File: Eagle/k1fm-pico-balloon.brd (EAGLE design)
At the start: 26.4 x 41.1 mm, 40 parts, among them Q1 ASTX-H11-25.000MHZ-T, Q2 DMP2305U, Q3 DMP2305U, U1 ATMEGA328, U2 Si5351A-B-GT, U3 MCP1754X-XXXXX/C, U4 TMP36, Y1 8/16/20MHz

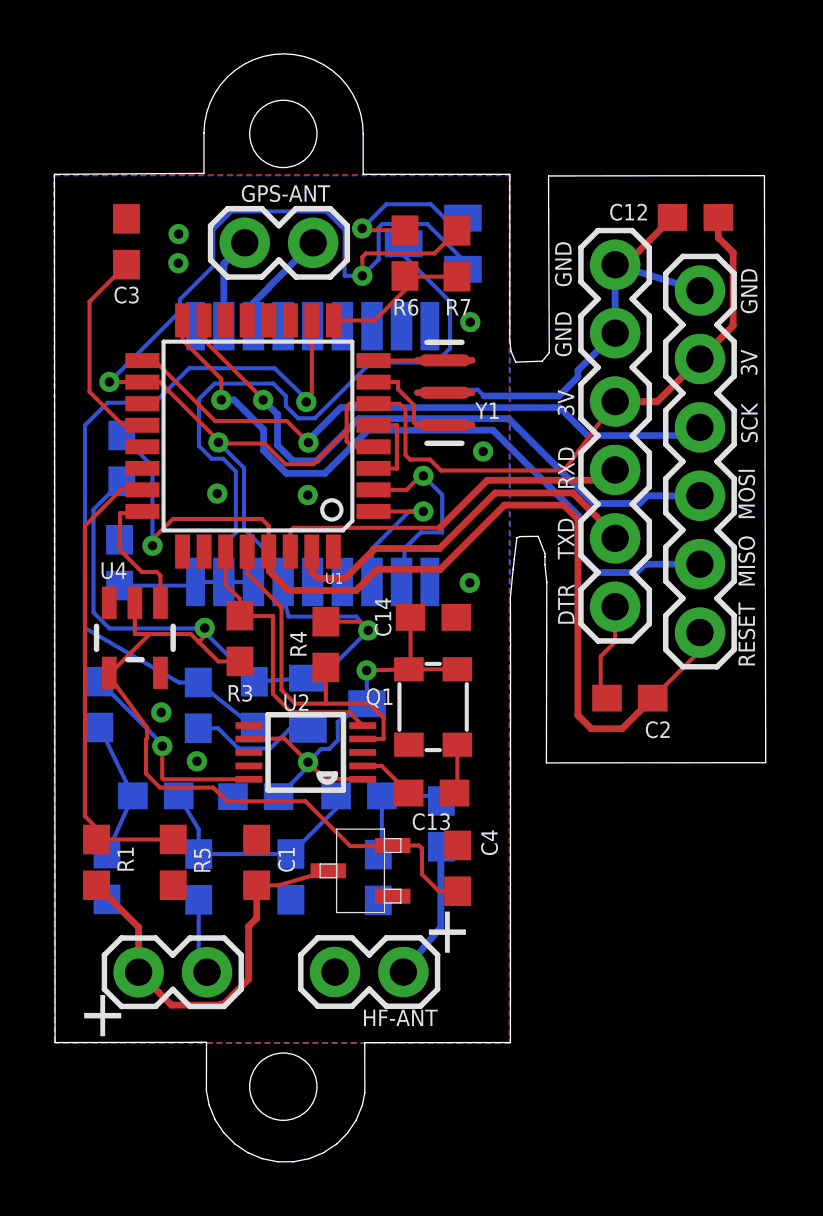
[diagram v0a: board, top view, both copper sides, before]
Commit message: 4 Layers. Added external SCL, SDA, GPS lines.
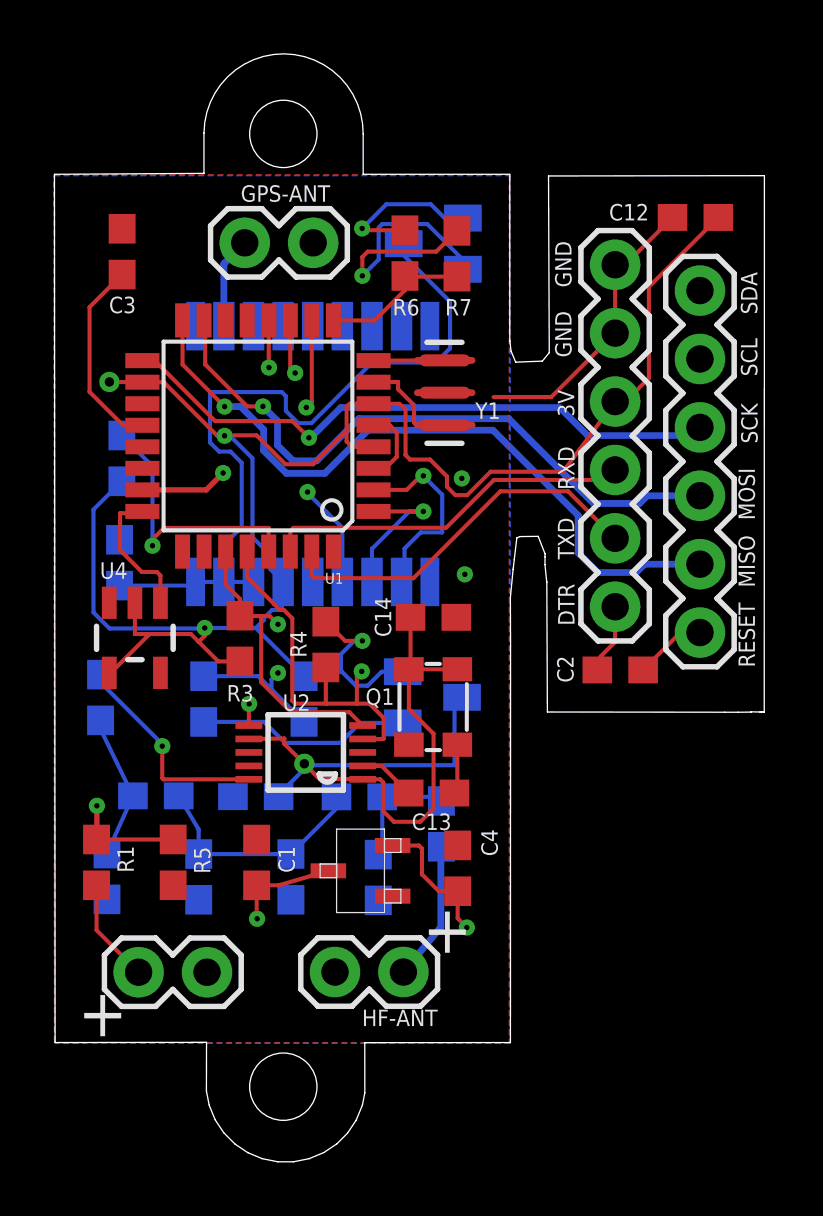
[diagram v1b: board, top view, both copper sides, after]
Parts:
- moved Q3 3.53 mm to (13.0, 60.6)
- moved R9 1.86 mm to (8.27, 60.5)
- moved C2 1.11 mm to (20.0, 61.6)
- moved C3 0.40 mm to (1.51, 77.1)
- moved R8 0.31 mm to (4.55, 60.5)
- moved L1 0.27 mm to (0.71, 60.6)
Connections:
- new net B0: GPS1.4_TIMEPULSE, U1.12
- new net D7: U1.11, U2.6
- net 3V: no longer J3.2
- net GND: no longer J3.1
- net SCL: now also J3.2
- net SDA: now also J3.1
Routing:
- net SDA: track 10.5 -> 36.1 mm, vias 0 -> 1
- net SCL: track 12.8 -> 36.4 mm, vias 0 -> 1
- net D7: track 0.00 -> 16.3 mm, vias 0 -> 2
- net GND: track 27.1 -> 13.8 mm, vias 9 -> 2
- net N$15: track 16.6 -> 28.2 mm, vias 2 -> 1
- net B0: track 0.00 -> 10.8 mm, vias 0 -> 2
- net TX_E: track 27.8 -> 19.9 mm, vias 1 -> 2
- net N$4: track 17.4 -> 22.1 mm, vias 0 -> 2
- net N$7: track 4.68 -> 8.02 mm
- net VDD: track 15.2 -> 13.2 mm, vias 0 -> 1
- net DTR: track 3.71 -> 2.62 mm
- net N$12: track 5.19 -> 6.26 mm
- net 3V: track 118.2 -> 118.4 mm, vias 5 -> 6
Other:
- outline, holes or cut-outs redrawn
- board text added: "K1FM v 1.3"
- board text added: "SCL"
- board text added: "SDA"
- board text removed: "K1FM v 1.2"

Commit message: Reorganized TX/RX lines - Conn layout
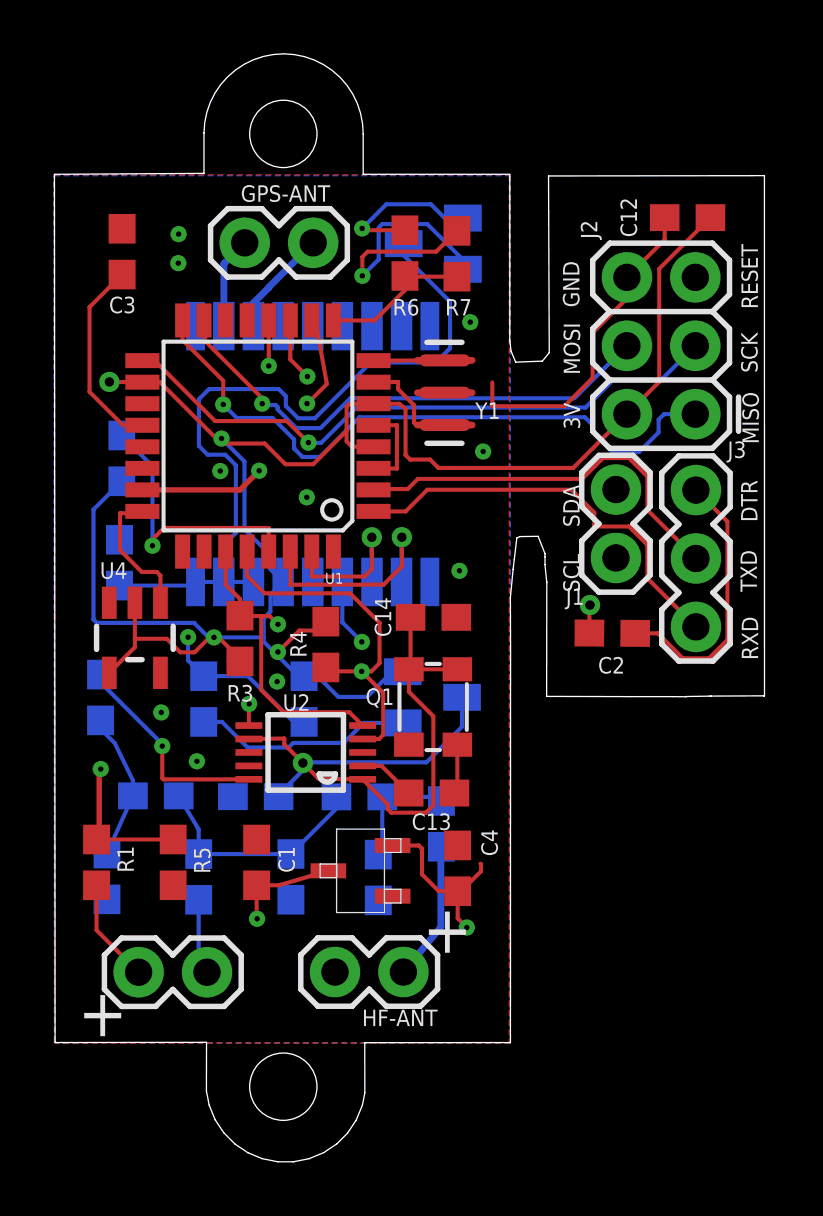
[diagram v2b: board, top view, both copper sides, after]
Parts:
- added J1: I2C, SparkFun-Connectors:1X02
- J2: value (none) -> ICSP; device SparkFun-Connectors:1X06 -> SparkFun-Connectors:2X3
- J3: value (none) -> SERIAL; device SparkFun-Connectors:1X06 -> SparkFun-Connectors:1X03
- moved J2 7.75 mm to (22.8, 71.1)
- moved J3 7.41 mm to (22.8, 68.3)
- moved C2 1.39 mm to (19.7, 63.0), turned to 179.6 degrees
- moved C12 0.29 mm to (22.5, 78.4)
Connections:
- net B0 renamed TIMEP
- net D7 renamed CLK2
- removed net D3: GPS1.3_RXD1, U1.1
- removed net D4: GPS1.2_TXD1, U1.2
- new net RXD: GPS1.2_TXD1, U1.30
- new net TXD: GPS1.3_RXD1, U1.31
- net 3V: now also J2.2; no longer J2.4
- net DTR: now also J3.1; no longer J2.1
- net GND: no longer J2.5
- net MISO: now also J2.1; no longer J3.5
- net MOSI: now also J2.4; no longer J3.4
- net RESET: now also J2.5; no longer J3.6
- net RXI: now also J3.3, U1.1; no longer J2.3, U1.30
- net SCK: now also J2.3; no longer J3.3
- net SCL: now also J1.2; no longer J3.2
- net SDA: now also J1.1; no longer J3.1
- net TXO: now also J3.2, U1.2; no longer J2.2, U1.31
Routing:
- net 3V: track 118.4 -> 139.0 mm
- net TIMEP: track 10.8 -> 24.6 mm
- net GND: track 13.8 -> 23.7 mm, vias 2 -> 10
- net SDA: track 36.1 -> 26.6 mm
- net SCL: track 36.4 -> 27.5 mm
- net TX_E: track 19.9 -> 28.6 mm
- net RXD: track 0.00 -> 8.56 mm, vias 0 -> 1
- net DTR: track 2.62 -> 10.1 mm
- net D4: track 7.39 -> 0.00 mm, vias 1 -> 0
- net TXD: track 0.00 -> 6.09 mm, vias 0 -> 1
- net RESET: track 38.4 -> 44.2 mm, vias 1 -> 2
- net D3: track 5.56 -> 0.00 mm, vias 1 -> 0
- net MOSI: track 24.1 -> 19.2 mm
- net MISO: track 26.8 -> 24.4 mm
- net N$4: track 22.1 -> 24.2 mm
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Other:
- outline, holes or cut-outs redrawn
- board text removed: "RST"
- board text removed: "VCC"

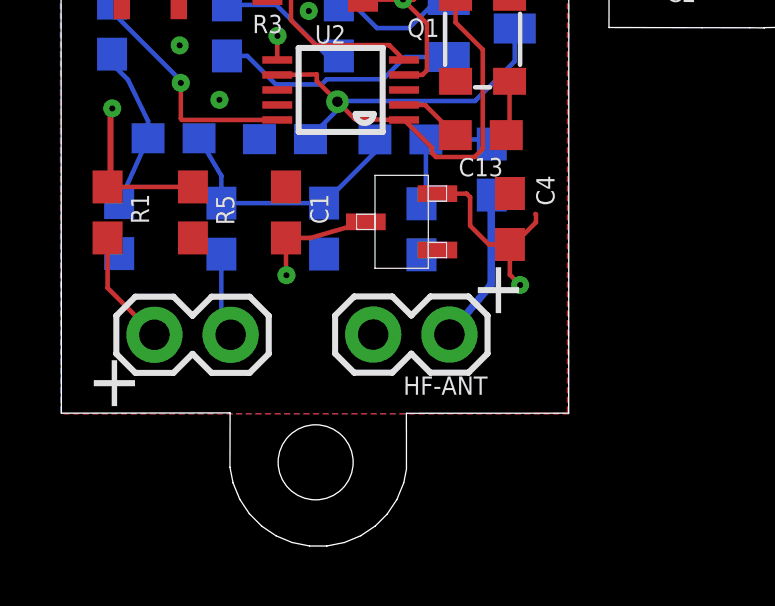
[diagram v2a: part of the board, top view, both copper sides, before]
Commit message: Add diode and connection for direct solar power
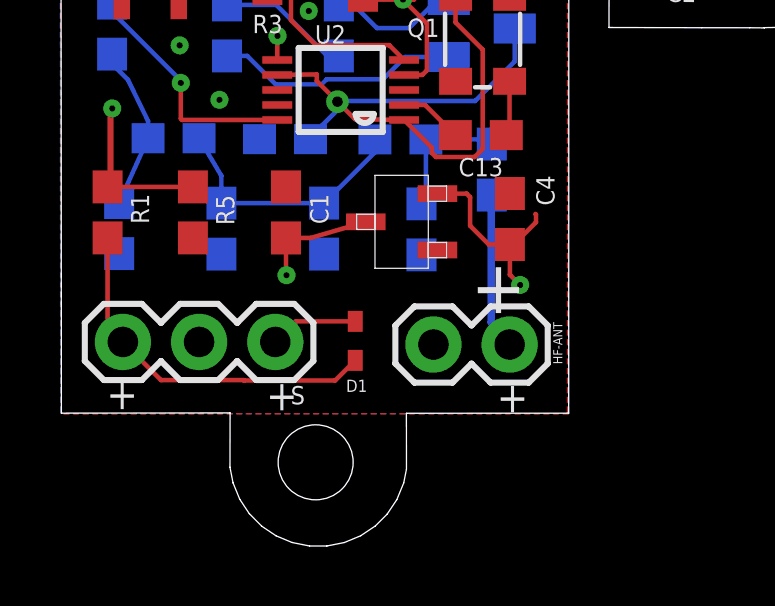
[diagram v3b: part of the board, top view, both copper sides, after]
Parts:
- removed 3.3V: 3.3V, SparkFun-Connectors:1X02
- added D1: 1N4148X-TP, diode:SOD523
- added J4: POWER, SparkFun-Connectors:1X03
- moved HF-ANT 2.03 mm to (14.0, 50.0)
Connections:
- new net N$3: D1.A, J4.3
- net GND: now also J4.2; no longer 3.3V.2
- net VDD: now also D1.C, J4.1; no longer 3.3V.1
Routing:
- net VDD: track 13.2 -> 22.7 mm
- net N$3: track 0.00 -> 2.95 mm
- net GND: track 23.7 -> 20.9 mm
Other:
- board text added: "S"
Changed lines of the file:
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@@
 <wire x1="4.553053125" y1="80.0339625" x2="-1" y2="80" width="0" layer="20"/>
 <wire x1="-1" y1="80" x2="-0.975784375" y2="47.755840625" width="0" layer="20"/>
-<text x="-0.12739375" y="47.991096875" size="1.778" layer="25">+</text>
+<text x="0.5252" y="47.889196875" size="1.016" layer="25">+</text>
 <text x="21.36460625" y="70.45336875" size="1.27" layer="26" rot="MR270" align="center">REMOVE
 BEFORE
 FLIGHT</text>
-<text x="13.09675" y="49.125609375" size="1.016" layer="26" rot="MR90">K1FM
+<text x="12.892821875" y="52.08070625" size="1.016" layer="26" rot="MR90">K1FM
 v 1.3</text>
 <wire x1="4.553053125" y1="80.0339625" x2="4.553053125" y2="81.5339625" width="0" layer="20"/>
@@
 <hole x="7.4994125" y="46.1168625" drill="2.5"/>
 <text x="12.67260625" y="51.091096875" size="1.778" layer="25">+</text>
+<text x="5.847759375" y="47.848434375" size="1.016" layer="25">+</text>
+<text x="13.5358875" y="47.787309375" size="1.016" layer="25">+</text>
+<text x="6.666075" y="48.049109375" size="0.6096" layer="21">S</text>
 </plain>
 <attributes>
@@
 </element>
 <element name="C7" library="SparkFun-Capacitors" library_urn="urn:adsk.eagle:library:510" package="0603" package3d_urn="urn:adsk.eagle:package:37414/1" value="47pF" x="7.7810625" y="53.907934375" smashed="yes" rot="MR90">
-<attribute name="NAME" x="7.795859375" y="51.543271875" size="0.6096" layer="26" font="vector" ratio="20" rot="MR0" align="bottom-center"/>
+<attribute name="NAME" x="7.829840625" y="51.543271875" size="0.6096" layer="26" font="vector" ratio="20" rot="MR0" align="bottom-center"/>
 <attribute name="PROD_ID" value="CAP-08604" x="-23.9689375" y="84.387934375" size="1.778" layer="28" rot="MR90" display="off"/>
 <attribute name="VALUE" x="7.0190625" y="53.907934375" size="0.6096" layer="28" font="vector" ratio="20" rot="MR90" align="top-center"/>
@@
 </element>
 <element name="GPS1" library="Ava" package="UBLOX_MAX" value="UBLOX_MAX" x="8.54139375" y="69.8114625" smashed="yes" rot="MR270"/>
-<element name="3.3V" library="SparkFun-Connectors" library_urn="urn:adsk.eagle:library:513" package="1X02" package3d_urn="urn:adsk.eagle:package:38039/1" value="3.3V" x="2.12581875" y="50.367578125" smashed="yes">
-<attribute name="VALUE" x="2.587046875" y="48.2646375" size="0.6096" layer="27" font="vector" ratio="20"/>
-</element>
 <element name="GPS-ANT" library="SparkFun-Connectors" library_urn="urn:adsk.eagle:library:513" package="1X02" package3d_urn="urn:adsk.eagle:package:38039/1" value="GPS ANT" x="8.6076125" y="77.45479375" smashed="yes" rot="R180">
 <attribute name="NAME" x="9.239053125" y="79.590609375" size="0.6096" layer="25" font="vector" ratio="20" rot="R180"/>
@@
 <attribute name="VALUE" x="13.004925" y="57.78485" size="0.6096" layer="27" font="vector" ratio="20" rot="R180" align="top-center"/>
 </element>
-<element name="HF-ANT" library="SparkFun-Connectors" library_urn="urn:adsk.eagle:library:513" package="1X02" package3d_urn="urn:adsk.eagle:package:38039/1" value="HF ANT" x="11.95895" y="50.374421875" smashed="yes" rot="R180">
-<attribute name="NAME" x="13.22895" y="48.977421875" size="0.6096" layer="25" font="vector" ratio="20" rot="R180"/>
-<attribute name="VALUE" x="13.22895" y="52.406421875" size="0.6096" layer="27" font="vector" ratio="20" rot="R180"/>
+<element name="HF-ANT" library="SparkFun-Connectors" library_urn="urn:adsk.eagle:library:513" package="1X02" package3d_urn="urn:adsk.eagle:package:38039/1" value="HF ANT" x="13.966375" y="50.042946875" smashed="yes" rot="R180">
+<attribute name="NAME" x="15.418203125" y="50.789784375" size="0.3048" layer="25" font="vector" ratio="20" rot="R270"/>
+<attribute name="VALUE" x="15.236375" y="52.074946875" size="0.6096" layer="27" font="vector" ratio="20" rot="R180"/>
 </element>
 <element name="Q3" library="transistor-fet" package="SOT23" value="DMP2305U" x="13.0356375" y="60.57650625" smashed="yes" rot="MR90">
@@
 <attribute name="NAME" x="23.99595625" y="69.46565" size="0.6096" layer="25" font="vector" ratio="20"/>
 <attribute name="VALUE" x="20.7908375" y="69.542840625" size="0.6096" layer="27" font="vector" ratio="20" rot="R270"/>
+</element>
+<element name="D1" library="diode" library_urn="urn:adsk.eagle:library:210" package="SOD523" package3d_urn="urn:adsk.eagle:package:43410/1" value="1N4148X-TP" x="8.8201875" y="50.115053125" smashed="yes" rot="R90">
+<attribute name="NAME" x="9.2179375" y="48.870134375" size="0.4064" layer="25" rot="R180"/>
+<attribute name="VALUE" x="10.7251875" y="49.480053125" size="1.27" layer="27" rot="R90"/>
+</element>
+<element name="J4" library="SparkFun-Connectors" library_urn="urn:adsk.eagle:library:513" package="1X03" package3d_urn="urn:adsk.eagle:package:38063/1" value="POWER" x="1.074065625" y="50.128775" smashed="yes">
+<attribute name="VALUE" x="-0.195934375" y="48.096775" size="0.6096" layer="27" font="vector" ratio="20"/>
 </element>
 </elements>
@@
 <contactref element="GPS1" pad="12_GND"/>
 <contactref element="GPS1" pad="1_GND"/>
-<contactref element="3.3V" pad="2"/>
 <contactref element="C3" pad="1"/>
 <contactref element="Y1" pad="2"/>
@@
 <contactref element="GPS1" pad="15_RESERVED"/>
 <contactref element="Q1" pad="2"/>
-<wire x1="4.356440625" y1="53.05499375" x2="4.356440625" y2="50.67695625" width="0.1524" layer="16"/>
-<wire x1="4.356440625" y1="50.67695625" x2="4.66581875" y2="50.367578125" width="0.1524" layer="16"/>
 <contactref element="C10" pad="2"/>
 <contactref element="R5" pad="1"/>
@@
 <wire x1="15.2606875" y1="71.386903125" x2="15.2606875" y2="72.268590625" width="0.1524" layer="1"/>
 <wire x1="18.986765625" y1="72.437053125" x2="17.936615625" y2="71.386903125" width="0.1524" layer="1"/>
+<contactref element="J4" pad="2"/>
 </signal>
 <signal name="3V">
@@
 <signal name="ANT">
 <contactref element="L3" pad="2"/>
-<wire x1="13.351559375" y1="52.047328125" x2="13.351559375" y2="55.00749375" width="0.254" layer="16"/>
+<wire x1="13.351559375" y1="50.781509375" x2="13.351559375" y2="55.00749375" width="0.254" layer="16"/>
 <wire x1="13.351559375" y1="55.00749375" x2="13.370315625" y2="55.02625" width="0.254" layer="16"/>
 <contactref element="HF-ANT" pad="1"/>
-<wire x1="11.95895" y1="50.374421875" x2="13.351559375" y2="52.047328125" width="0.254" layer="16"/>
+<wire x1="13.966375" y1="50.042946875" x2="13.351559375" y2="50.781509375" width="0.254" layer="16"/>
 </signal>
 <signal name="N$12">
@@
 </signal>
 <signal name="VDD">
-<contactref element="3.3V" pad="1"/>
 <contactref element="C1" pad="1"/>
 <contactref element="U3" pad="3"/>
@@
 <wire x1="6.510471875" y1="53.595575" x2="7.33501875" y2="53.595575" width="0.1524" layer="1"/>
 <wire x1="7.33501875" y1="53.595575" x2="9.17271875" y2="54.132665625" width="0.1524" layer="1"/>
-<wire x1="0.56444375" y1="53.59650625" x2="0.56444375" y2="51.928953125" width="0.1524" layer="1"/>
-<wire x1="0.56444375" y1="51.928953125" x2="2.12581875" y2="50.367578125" width="0.1524" layer="1"/>
 <wire x1="6.510471875" y1="53.595575" x2="6.510471875" y2="52.368921875" width="0.1524" layer="1"/>
 <wire x1="6.510471875" y1="52.368921875" x2="6.526465625" y2="52.352928125" width="0.1524" layer="1"/>
 <via x="6.526465625" y="52.352928125" extent="1-16" drill="0.2"/>
-<wire x1="6.526465625" y1="52.352928125" x2="6.03495" y2="51.8614125" width="0.1524" layer="2"/>
-<wire x1="6.03495" y1="51.8614125" x2="3.5091375" y2="51.8614125" width="0.1524" layer="2"/>
-<wire x1="3.5091375" y1="51.8614125" x2="2.12581875" y2="50.47809375" width="0.1524" layer="2"/>
-<wire x1="2.12581875" y1="50.47809375" x2="2.12581875" y2="50.367578125" width="0.1524" layer="2"/>
+<contactref element="D1" pad="C"/>
+<contactref element="J4" pad="1"/>
+<wire x1="1.074065625" y1="50.128775" x2="0.56444375" y2="50.638396875" width="0.1524" layer="1"/>
+<wire x1="0.56444375" y1="50.638396875" x2="0.56444375" y2="53.59650625" width="0.1524" layer="1"/>
+<wire x1="6.526465625" y1="52.352928125" x2="6.04241875" y2="51.86888125" width="0.1524" layer="2"/>
+<wire x1="6.04241875" y1="51.86888125" x2="2.6530375" y2="51.86888125" width="0.1524" layer="2"/>
+<wire x1="2.6530375" y1="51.86888125" x2="1.074065625" y2="50.289909375" width="0.1524" layer="2"/>
+<wire x1="1.074065625" y1="50.289909375" x2="1.074065625" y2="50.128775" width="0.1524" layer="2"/>
+<wire x1="1.074065625" y1="50.128775" x2="2.34605625" y2="48.856784375" width="0.1524" layer="1"/>
+<wire x1="2.34605625" y1="48.856784375" x2="5.1015625" y2="48.856784375" width="0.1524" layer="1"/>
+<wire x1="5.1015625" y1="48.856784375" x2="5.11453125" y2="48.843815625" width="0.1524" layer="1"/>
+<wire x1="8.14895" y1="48.843815625" x2="8.8201875" y2="49.515053125" width="0.1524" layer="1"/>
+<wire x1="5.11453125" y1="48.843815625" x2="8.14895" y2="48.843815625" width="0.1524" layer="1"/>
 </signal>
 <signal name="N$4">
@@
 <wire x1="9.69139375" y1="64.8614625" x2="9.69139375" y2="63.35839375" width="0.1524" layer="16"/>
 </signal>
+<signal name="N$3">
+<contactref element="D1" pad="A"/>
+<contactref element="J4" pad="3"/>
+<wire x1="6.154065625" y1="50.128775" x2="6.84034375" y2="50.815053125" width="0.1524" layer="1"/>
+<wire x1="6.84034375" y1="50.815053125" x2="8.8201875" y2="50.815053125" width="0.1524" layer="1"/>
+</signal>
 </signals>
